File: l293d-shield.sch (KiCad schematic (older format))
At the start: 3 parts, among them J1 Screw_Terminal_1x04, U1 l293d

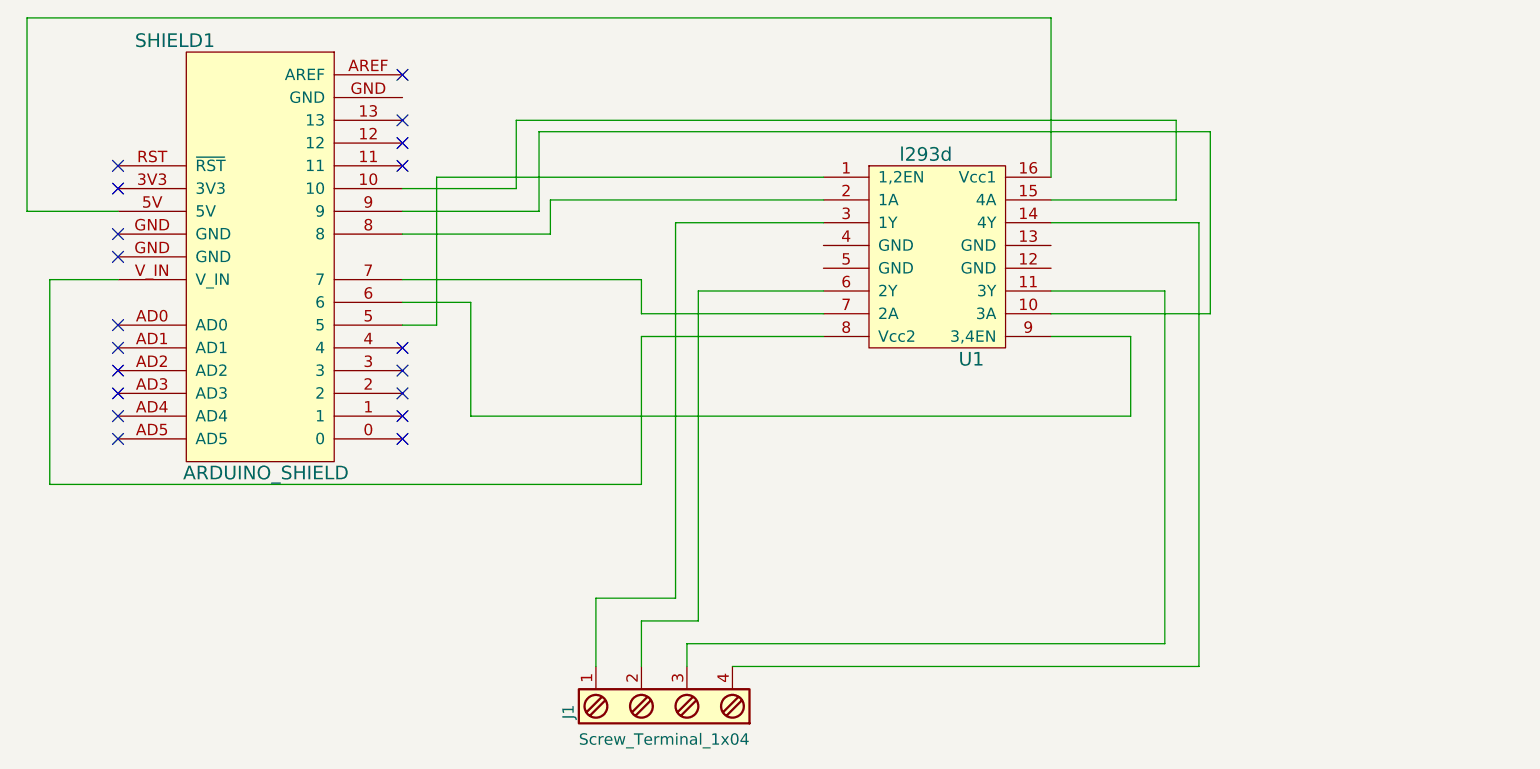
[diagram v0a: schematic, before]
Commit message: Improve schematic layout
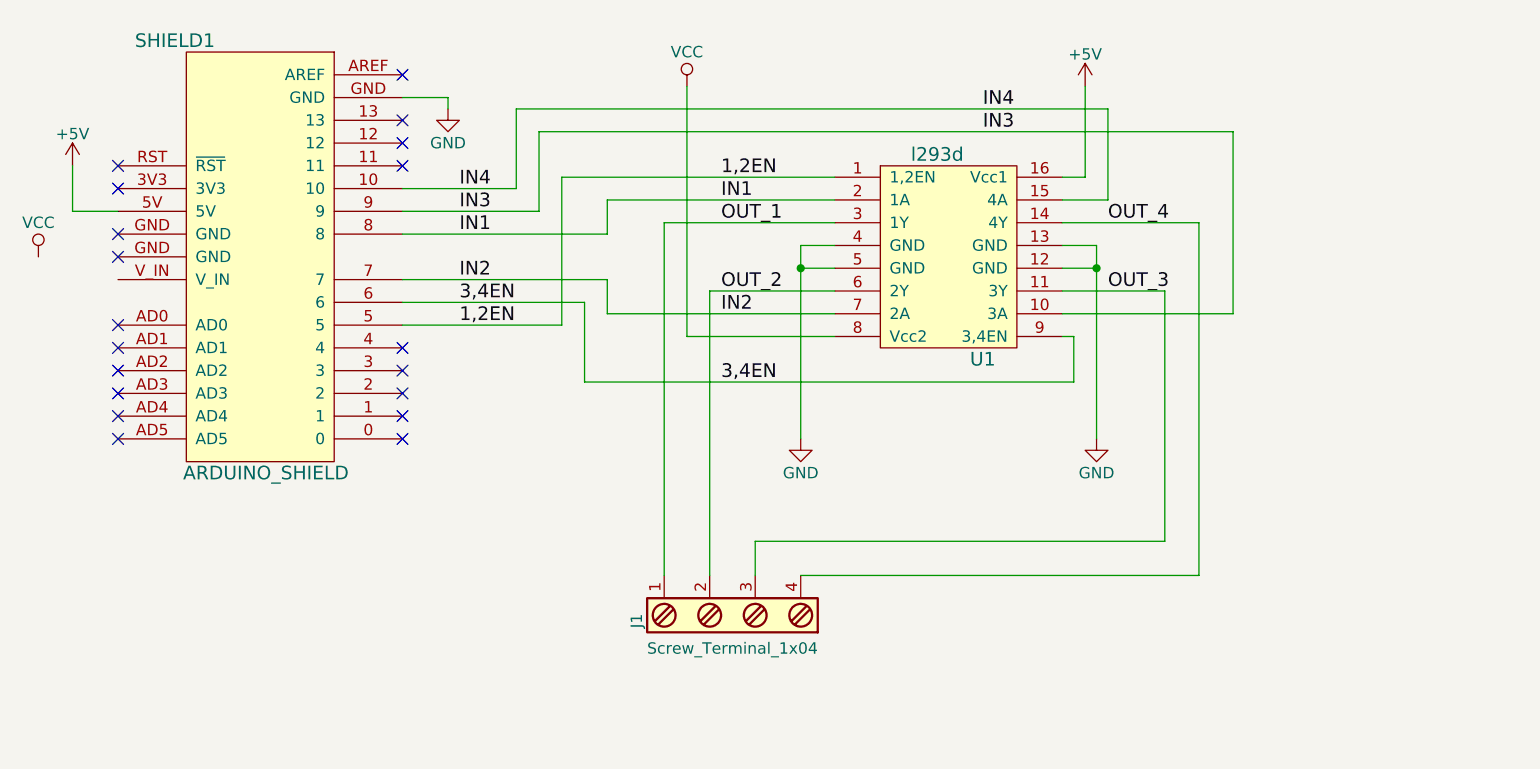
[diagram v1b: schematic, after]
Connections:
- net IN4: now reaches SHIELD1.10, U1.15 (4A)
- net 1,2EN: now reaches SHIELD1.5, U1.1 (1,2EN)
- net +5V: now reaches SHIELD1.5V, U1.16 (Vcc1)
- net 3,4EN: now reaches SHIELD1.6, U1.9 (3,4EN)
- net IN2: now reaches SHIELD1.7, U1.7 (2A)
- net IN1: now reaches SHIELD1.8, U1.2 (1A)
- net IN3: now reaches SHIELD1.9, U1.10 (3A)
- net GND: now reaches SHIELD1.GND
- net GND: now also U1.12 (GND), U1.13 (GND), U1.4 (GND), U1.5 (GND)
- net at SHIELD1.V_IN: no longer U1.8 (Vcc2)
- net OUT_1: now reaches J1.1, U1.3 (1Y)
- net OUT_2: now reaches J1.2, U1.6 (2Y)
- net OUT_3: now reaches J1.3, U1.11 (3Y)
- net OUT_4: now reaches J1.4, U1.14 (4Y)
- new net VCC: U1.8 (Vcc2)
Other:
- moved on the sheet: J1, U1
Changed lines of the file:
@@
 L Screw_Terminal_1x04 J1
 U 1 1 593CEB9B
-P 4000 4700
-F 0 "J1" H 4000 5150 50  0000 C TNN
-F 1 "Screw_Terminal_1x04" V 3850 4700 50  0000 C TNN
-F 2 "Connectors_Terminal_Blocks:TerminalBlock_Pheonix_MKDS1.5-4pol" H 4000 4275 50  0001 C CNN
-F 3 "" H 3975 4900 50  0001 C CNN
-	1    4000 4700
+P 4300 4300
+F 0 "J1" H 4300 4750 50  0000 C TNN
+F 1 "Screw_Terminal_1x04" V 4150 4300 50  0000 C TNN
+F 2 "Connectors_Terminal_Blocks:TerminalBlock_Pheonix_MKDS1.5-4pol" H 4300 3875 50  0001 C CNN
+F 3 "" H 4275 4500 50  0001 C CNN
+	1    4300 4300
 	0    -1   -1   0
 $EndComp
@@
 NoConn ~ 1600 3400
 NoConn ~ 1600 3500
-Wire Wire Line
-	2850 3000 3000 3000
-Wire Wire Line
-	3000 3000 3000 2350
-Wire Wire Line
-	3000 2350 4700 2350
-Wire Wire Line
-	2850 2900 3150 2900
-Wire Wire Line
-	3150 2900 3150 3400
-Wire Wire Line
-	3150 3400 6050 3400
-Wire Wire Line
-	6050 3400 6050 3050
-Wire Wire Line
-	6050 3050 5700 3050
-Wire Wire Line
-	4300 4500 6350 4500
-Wire Wire Line
-	6350 4500 6350 2550
-Wire Wire Line
-	6350 2550 5700 2550
-Wire Wire Line
-	4100 4500 4100 4400
-Wire Wire Line
-	4100 4400 6200 4400
-Wire Wire Line
-	6200 4400 6200 2850
-Wire Wire Line
-	6200 2850 5700 2850
-Wire Wire Line
-	3900 4500 3900 4300
-Wire Wire Line
-	3900 4300 4150 4300
-Wire Wire Line
-	4150 4300 4150 2850
-Wire Wire Line
-	4150 2850 4700 2850
-Wire Wire Line
-	3700 4500 3700 4200
-Wire Wire Line
-	3700 4200 4050 4200
-Wire Wire Line
-	4050 4200 4050 2550
-Wire Wire Line
-	4050 2550 4700 2550
-Wire Wire Line
-	2850 2800 3900 2800
-Wire Wire Line
-	3900 2800 3900 2950
-Wire Wire Line
-	3900 2950 4700 2950
-Wire Wire Line
-	2850 2600 3500 2600
-Wire Wire Line
-	3500 2600 3500 2450
-Wire Wire Line
-	3500 2450 4700 2450
-Wire Wire Line
-	2850 2500 3450 2500
-Wire Wire Line
-	3450 2500 3450 2150
-Wire Wire Line
-	3450 2150 6400 2150
-Wire Wire Line
-	6400 2150 6400 2950
-Wire Wire Line
-	6400 2950 5700 2950
-Wire Wire Line
-	2850 2400 3350 2400
-Wire Wire Line
-	3350 2400 3350 2100
-Wire Wire Line
-	3350 2100 6250 2100
-Wire Wire Line
-	6250 2100 6250 2450
-Wire Wire Line
-	6250 2450 5700 2450
-Wire Wire Line
-	1600 2500 1200 2500
-Wire Wire Line
-	1200 2500 1200 1650
-Wire Wire Line
-	1200 1650 5700 1650
-Wire Wire Line
-	1600 2800 1300 2800
-Wire Wire Line
-	1300 2800 1300 3700
-Wire Wire Line
-	1300 3700 3900 3700
-Wire Wire Line
-	3900 3700 3900 3050
-Wire Wire Line
-	3900 3050 4700 3050
 NoConn ~ 1600 2400
 NoConn ~ 1600 2300
@@
 NoConn ~ 2850 2100
 NoConn ~ 2850 1900
-Wire Wire Line
-	5700 1650 5700 2350
 $Comp
 L l293d U1
 U 1 1 593D9784
-P 5550 3050
-F 0 "U1" H 5350 2950 60  0000 C CNN
-F 1 "l293d" H 5150 3850 60  0000 C CNN
-F 2 "Housings_DIP:DIP-16_W7.62mm" H 5850 2850 60  0001 C CNN
-F 3 "" H 5850 2850 60  0001 C CNN
-	1    5550 3050
+P 5600 3050
+F 0 "U1" H 5400 2950 60  0000 C CNN
+F 1 "l293d" H 5200 3850 60  0000 C CNN
+F 2 "Housings_DIP:DIP-16_W7.62mm" H 5900 2850 60  0001 C CNN
+F 3 "" H 5900 2850 60  0001 C CNN
+	1    5600 3050
 	1    0    0    -1
 $EndComp
 NoConn ~ 1600 2700
 NoConn ~ 1600 2600
+$Comp
+L +5V #PWR?
+U 1 1 5940B942
+P 1400 2300
+F 0 "#PWR?" H 1400 2150 50  0001 C CNN
+F 1 "+5V" H 1400 2440 50  0000 C CNN
+F 2 "" H 1400 2300 50  0001 C CNN
+F 3 "" H 1400 2300 50  0001 C CNN
+	1    1400 2300
+	1    0    0    -1
+$EndComp
+$Comp
+L VCC #PWR?
+U 1 1 5940B95C
+P 1250 2700
+F 0 "#PWR?" H 1250 2550 50  0001 C CNN
+F 1 "VCC" H 1250 2850 50  0000 C CNN
+F 2 "" H 1250 2700 50  0001 C CNN
+F 3 "" H 1250 2700 50  0001 C CNN
+	1    1250 2700
+	1    0    0    -1
+$EndComp
+$Comp
+L GND #PWR?
+U 1 1 5940B976
+P 3050 2050
+F 0 "#PWR?" H 3050 1800 50  0001 C CNN
+F 1 "GND" H 3050 1900 50  0000 C CNN
+F 2 "" H 3050 2050 50  0001 C CNN
+F 3 "" H 3050 2050 50  0001 C CNN
+	1    3050 2050
+	1    0    0    -1
+$EndComp
+$Comp
+L GND #PWR?
+U 1 1 5940B990
+P 4600 3500
+F 0 "#PWR?" H 4600 3250 50  0001 C CNN
+F 1 "GND" H 4600 3350 50  0000 C CNN
+F 2 "" H 4600 3500 50  0001 C CNN
+F 3 "" H 4600 3500 50  0001 C CNN
+	1    4600 3500
+	1    0    0    -1
+$EndComp
+$Comp
+L GND #PWR?
+U 1 1 5940B9AA
+P 5900 3500
+F 0 "#PWR?" H 5900 3250 50  0001 C CNN
+F 1 "GND" H 5900 3350 50  0000 C CNN
+F 2 "" H 5900 3500 50  0001 C CNN
+F 3 "" H 5900 3500 50  0001 C CNN
+	1    5900 3500
+	1    0    0    -1
+$EndComp
+Text Label 3100 2900 0    60   ~ 0
+3,4EN
+Text Label 3100 3000 0    60   ~ 0
+1,2EN
+$Comp
+L +5V #PWR?
+U 1 1 5940BBA9
+P 5850 1950
+F 0 "#PWR?" H 5850 1800 50  0001 C CNN
+F 1 "+5V" H 5850 2090 50  0000 C CNN
+F 2 "" H 5850 1950 50  0001 C CNN
+F 3 "" H 5850 1950 50  0001 C CNN
+	1    5850 1950
+	1    0    0    -1
+$EndComp
+Text Label 4250 2550 0    60   ~ 0
+OUT_1
+Text Label 4250 2850 0    60   ~ 0
+OUT_2
+Text Label 5950 2850 0    60   ~ 0
+OUT_3
+Text Label 5950 2550 0    60   ~ 0
+OUT_4
+$Comp
+L VCC #PWR?
+U 1 1 5940C07A
+P 4100 1950
+F 0 "#PWR?" H 4100 1800 50  0001 C CNN
+F 1 "VCC" H 4100 2100 50  0000 C CNN
+F 2 "" H 4100 1950 50  0001 C CNN
+F 3 "" H 4100 1950 50  0001 C CNN
+	1    4100 1950
+	1    0    0    -1
+$EndComp
+Wire Wire Line
+	2850 3000 3550 3000
+Wire Wire Line
+	3550 3000 3550 2350
+Wire Wire Line
+	3550 2350 4750 2350
+Wire Wire Line
+	2850 2900 3650 2900
+Wire Wire Line
+	3650 2900 3650 3250
+Wire Wire Line
+	3650 3250 5800 3250
+Wire Wire Line
+	5750 3050 5800 3050
+Wire Wire Line
+	6350 2550 5750 2550
+Wire Wire Line
+	6200 2850 5750 2850
+Wire Wire Line
+	4200 2850 4200 4100
+Wire Wire Line
+	4200 2850 4750 2850
+Wire Wire Line
+	4000 2550 4000 4100
+Wire Wire Line
+	4000 2550 4750 2550
+Wire Wire Line
+	2850 2800 3750 2800
+Wire Wire Line
+	3750 2800 3750 2950
+Wire Wire Line
+	3750 2950 4750 2950
+Wire Wire Line
+	2850 2600 3750 2600
+Wire Wire Line
+	3750 2600 3750 2450
+Wire Wire Line
+	3750 2450 4750 2450
+Wire Wire Line
+	2850 2400 3350 2400
+Wire Wire Line
+	3350 2400 3350 2050
+Wire Wire Line
+	3350 2050 5950 2050
+Wire Wire Line
+	5950 2050 5950 2450
+Wire Wire Line
+	5950 2450 5750 2450
+Wire Wire Line
+	2850 2000 3050 2000
+Wire Wire Line
+	3050 2000 3050 2050
+Wire Wire Line
+	4750 2650 4600 2650
+Wire Wire Line
+	4600 2650 4600 2750
+Wire Wire Line
+	4600 2750 4600 3500
+Wire Wire Line
+	4750 2750 4600 2750
+Connection ~ 4600 2750
+Wire Wire Line
+	5750 2650 5900 2650
+Wire Wire Line
+	5900 2650 5900 2750
+Wire Wire Line
+	5900 2750 5900 3500
+Wire Wire Line
+	5750 2750 5900 2750
+Connection ~ 5900 2750
+Wire Wire Line
+	5750 2350 5850 2350
+Wire Wire Line
+	5850 2350 5850 1950
+Wire Wire Line
+	1400 2300 1400 2500
+Wire Wire Line
+	1400 2500 1600 2500
+Wire Wire Line
+	4100 3050 4750 3050
+Wire Wire Line
+	4100 1950 4100 3050
+Wire Wire Line
+	5800 3050 5800 3250
+Text Label 3100 2800 0    60   ~ 0
+IN2
+Text Label 3100 2600 0    60   ~ 0
+IN1
+Wire Wire Line
+	6500 2950 5750 2950
+Wire Wire Line
+	6500 2150 6500 2950
+Wire Wire Line
+	3450 2150 6500 2150
+Wire Wire Line
+	3450 2500 3450 2150
+Wire Wire Line
+	2850 2500 3450 2500
+Wire Wire Line
+	6200 2850 6200 3950
+Wire Wire Line
+	6200 3950 4400 3950
+Wire Wire Line
+	4400 3950 4400 4100
+Wire Wire Line
+	4600 4100 6350 4100
+Wire Wire Line
+	6350 4100 6350 2550
+Text Label 4250 3250 0    60   ~ 0
+3,4EN
+Text Label 4250 2350 0    60   ~ 0
+1,2EN
+Text Label 4250 2450 0    60   ~ 0
+IN1
+Text Label 4250 2950 0    60   ~ 0
+IN2
+Text Label 3100 2400 0    60   ~ 0
+IN4
+Text Label 3100 2500 0    60   ~ 0
+IN3
+Text Label 5400 2050 0    60   ~ 0
+IN4
+Text Label 5400 2150 0    60   ~ 0
+IN3
 $EndSCHEMATC

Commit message: Add battery connector and footprints
Add battery connector 1x2 .01" footprint
Add motor connector 1x4 .01" footprint
Fix global power nets in schematic
Add battery connector to shield
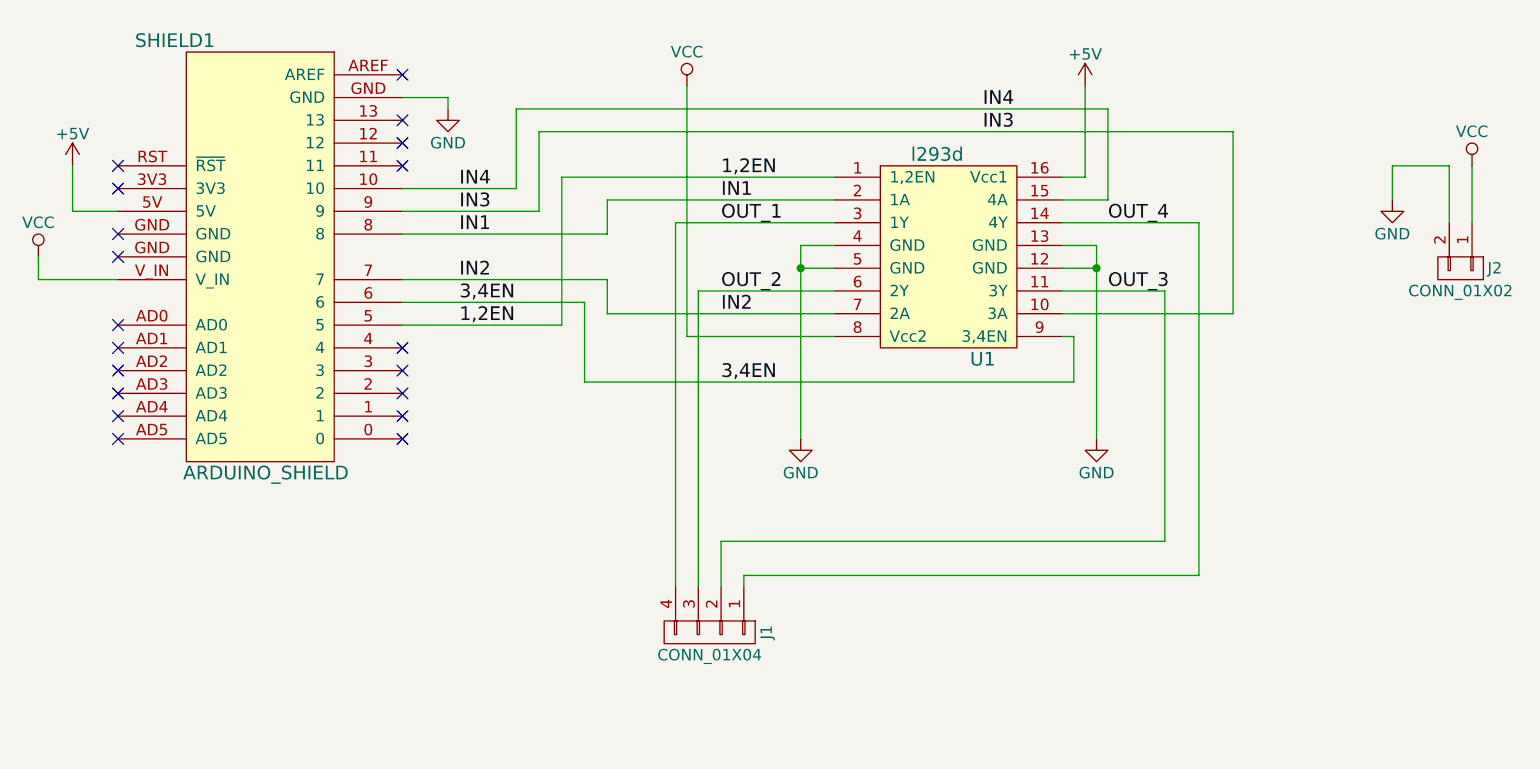
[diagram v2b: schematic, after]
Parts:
- removed J1: Screw_Terminal_1x04, Connectors_Terminal_Blocks:TerminalBlock_Pheonix_MKDS1.5-4pol, symbol Screw_Terminal_1x04
- added J1: CONN_01X04, Connectors_Molex:Molex_KK-6410-04_04x2.54mm_Straight, symbol CONN_01X04
- added J2: CONN_01X02, Connectors_Molex:Molex_KK-6410-02_02x2.54mm_Straight, symbol CONN_01X02
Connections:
- net GND: now also J2.2 (P2)
- net OUT_1: now also J1.4 (P4)
- net OUT_2: now also J1.3 (P3)
- net OUT_3: now also J1.2 (P2)
- net OUT_4: now also J1.1 (P1)
- net VCC: now also SHIELD1.V_IN, J2.1 (P1)
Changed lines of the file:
@@
 LIBS:valves
 LIBS:l293d-shield
+LIBS:l293d-shield-cache
 EELAYER 25 0
 EELAYER END
@@
 	1    2200 2700
 	1    0    0    -1
-$EndComp
-$Comp
-L Screw_Terminal_1x04 J1
-U 1 1 593CEB9B
-P 4300 4300
-F 0 "J1" H 4300 4750 50  0000 C TNN
-F 1 "Screw_Terminal_1x04" V 4150 4300 50  0000 C TNN
-F 2 "Connectors_Terminal_Blocks:TerminalBlock_Pheonix_MKDS1.5-4pol" H 4300 3875 50  0001 C CNN
-F 3 "" H 4275 4500 50  0001 C CNN
-	1    4300 4300
-	0    -1   -1   0
 $EndComp
 NoConn ~ 1600 3000
@@
 NoConn ~ 1600 2600
 $Comp
-L +5V #PWR?
+L +5V #PWR2
 U 1 1 5940B942
 P 1400 2300
-F 0 "#PWR?" H 1400 2150 50  0001 C CNN
+F 0 "#PWR2" H 1400 2150 50  0001 C CNN
 F 1 "+5V" H 1400 2440 50  0000 C CNN
 F 2 "" H 1400 2300 50  0001 C CNN
@@
 $EndComp
 $Comp
-L VCC #PWR?
+L VCC #PWR1
 U 1 1 5940B95C
 P 1250 2700
-F 0 "#PWR?" H 1250 2550 50  0001 C CNN
+F 0 "#PWR1" H 1250 2550 50  0001 C CNN
 F 1 "VCC" H 1250 2850 50  0000 C CNN
 F 2 "" H 1250 2700 50  0001 C CNN
@@
 $EndComp
 $Comp
-L GND #PWR?
+L GND #PWR3
 U 1 1 5940B976
 P 3050 2050
-F 0 "#PWR?" H 3050 1800 50  0001 C CNN
+F 0 "#PWR3" H 3050 1800 50  0001 C CNN
 F 1 "GND" H 3050 1900 50  0000 C CNN
 F 2 "" H 3050 2050 50  0001 C CNN
@@
 $EndComp
 $Comp
-L GND #PWR?
+L GND #PWR5
 U 1 1 5940B990
 P 4600 3500
-F 0 "#PWR?" H 4600 3250 50  0001 C CNN
+F 0 "#PWR5" H 4600 3250 50  0001 C CNN
 F 1 "GND" H 4600 3350 50  0000 C CNN
 F 2 "" H 4600 3500 50  0001 C CNN
@@
 $EndComp
 $Comp
-L GND #PWR?
+L GND #PWR7
 U 1 1 5940B9AA
 P 5900 3500
-F 0 "#PWR?" H 5900 3250 50  0001 C CNN
+F 0 "#PWR7" H 5900 3250 50  0001 C CNN
 F 1 "GND" H 5900 3350 50  0000 C CNN
 F 2 "" H 5900 3500 50  0001 C CNN
@@
 1,2EN
 $Comp
-L +5V #PWR?
+L +5V #PWR6
 U 1 1 5940BBA9
 P 5850 1950
-F 0 "#PWR?" H 5850 1800 50  0001 C CNN
+F 0 "#PWR6" H 5850 1800 50  0001 C CNN
 F 1 "+5V" H 5850 2090 50  0000 C CNN
 F 2 "" H 5850 1950 50  0001 C CNN
@@
 OUT_4
 $Comp
-L VCC #PWR?
+L VCC #PWR4
 U 1 1 5940C07A
 P 4100 1950
-F 0 "#PWR?" H 4100 1800 50  0001 C CNN
+F 0 "#PWR4" H 4100 1800 50  0001 C CNN
 F 1 "VCC" H 4100 2100 50  0000 C CNN
 F 2 "" H 4100 1950 50  0001 C CNN
@@
 	6200 2850 5750 2850
 Wire Wire Line
-	4200 2850 4200 4100
-Wire Wire Line
-	4200 2850 4750 2850
-Wire Wire Line
-	4000 2550 4000 4100
-Wire Wire Line
-	4000 2550 4750 2550
+	4150 2850 4150 4150
+Wire Wire Line
+	4150 2850 4750 2850
+Wire Wire Line
+	4050 2550 4050 4150
+Wire Wire Line
+	4050 2550 4750 2550
 Wire Wire Line
 	2850 2800 3750 2800
@@
 	4750 2650 4600 2650
 Wire Wire Line
-	4600 2650 4600 2750
-Wire Wire Line
-	4600 2750 4600 3500
+	4600 2650 4600 3500
 Wire Wire Line
 	4750 2750 4600 2750
@@
 	5750 2650 5900 2650
 Wire Wire Line
-	5900 2650 5900 2750
-Wire Wire Line
-	5900 2750 5900 3500
+	5900 2650 5900 3500
 Wire Wire Line
 	5750 2750 5900 2750
@@
 	6200 2850 6200 3950
 Wire Wire Line
-	6200 3950 4400 3950
-Wire Wire Line
-	4400 3950 4400 4100
-Wire Wire Line
-	4600 4100 6350 4100
+	6200 3950 4250 3950
+Wire Wire Line
+	4250 3950 4250 4150
+Wire Wire Line
+	4350 4100 6350 4100
 Wire Wire Line
 	6350 4100 6350 2550
@@
 Text Label 5400 2150 0    60   ~ 0
 IN3
+$Comp
+L CONN_01X04 J1
+U 1 1 59509D89
+P 4200 4350
+F 0 "J1" H 4200 4600 50  0000 C CNN
+F 1 "CONN_01X04" V 4300 4350 50  0000 C CNN
+F 2 "Connectors_Molex:Molex_KK-6410-04_04x2.54mm_Straight" H 4200 4350 50  0001 C CNN
+F 3 "" H 4200 4350 50  0001 C CNN
+	1    4200 4350
+	0    1    1    0
+$EndComp
+Wire Wire Line
+	4350 4100 4350 4150
+Wire Wire Line
+	1250 2700 1250 2800
+Wire Wire Line
+	1250 2800 1600 2800
+$Comp
+L CONN_01X02 J2
+U 1 1 595350F0
+P 7500 2750
+F 0 "J2" V 7500 2900 50  0000 C CNN
+F 1 "CONN_01X02" V 7600 2750 50  0000 C CNN
+F 2 "Connectors_Molex:Molex_KK-6410-02_02x2.54mm_Straight" H 7500 2750 50  0001 C CNN
+F 3 "" H 7500 2750 50  0001 C CNN
+	1    7500 2750
+	0    1    1    0
+$EndComp
+$Comp
+L VCC #PWR9
+U 1 1 595352BF
+P 7550 2300
+F 0 "#PWR9" H 7550 2150 50  0001 C CNN
+F 1 "VCC" H 7550 2450 50  0000 C CNN
+F 2 "" H 7550 2300 50  0001 C CNN
+F 3 "" H 7550 2300 50  0001 C CNN
+	1    7550 2300
+	1    0    0    -1
+$EndComp
+Wire Wire Line
+	7550 2300 7550 2550
+$Comp
+L GND #PWR8
+U 1 1 59535457
+P 7200 2450
+F 0 "#PWR8" H 7200 2200 50  0001 C CNN
+F 1 "GND" H 7200 2300 50  0000 C CNN
+F 2 "" H 7200 2450 50  0001 C CNN
+F 3 "" H 7200 2450 50  0001 C CNN
+	1    7200 2450
+	1    0    0    -1
+$EndComp
+Wire Wire Line
+	7200 2450 7200 2300
+Wire Wire Line
+	7200 2300 7450 2300
+Wire Wire Line
+	7450 2300 7450 2550
 $EndSCHEMATC
